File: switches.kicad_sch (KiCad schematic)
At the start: 9 parts, among them J13 Switch Assembly

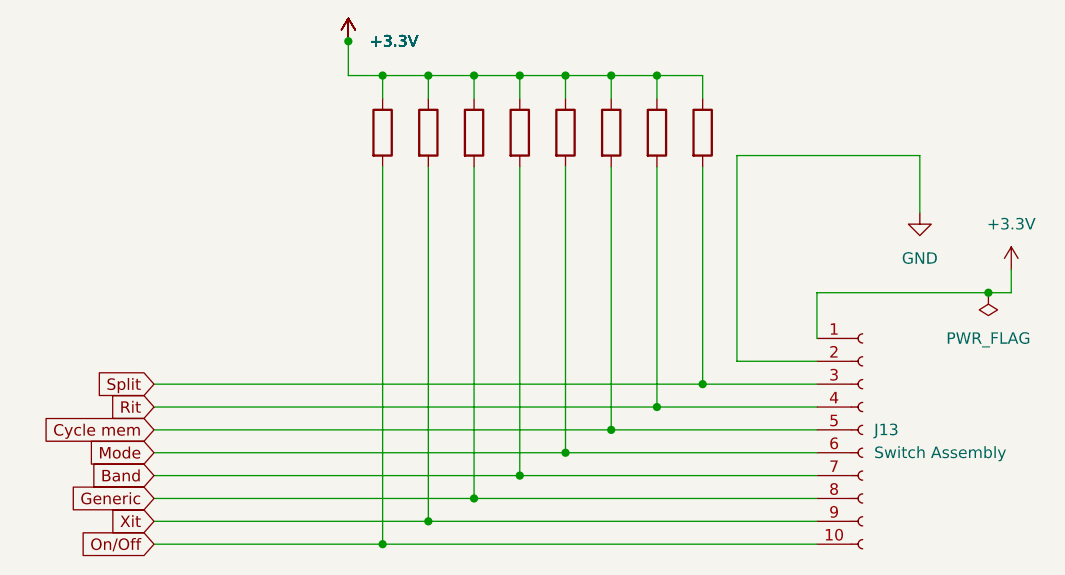
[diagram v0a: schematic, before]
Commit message: cont routing work
Changes:

* Added mounting holes
* Tried to trim down PCB size a litle more.
* Attempted to separate digital IO from analog.
* Added socket IC for RJ45 & 6P6C / RJ12 configurability.
* WIP: Add muxer for UART line switching.

Comment:

The muxer UART functionality isn't complete, the idea is to allow switching between using
the RJ45 RXD & TXD UART to the RJ12 / 6P6C UART lines.
Since the real rrc hardware supports this (depends on the radio configured) & maybe depending on socket strapping..
Need to add a jumper to enable switching between these, alternatively use a GPIO pin??
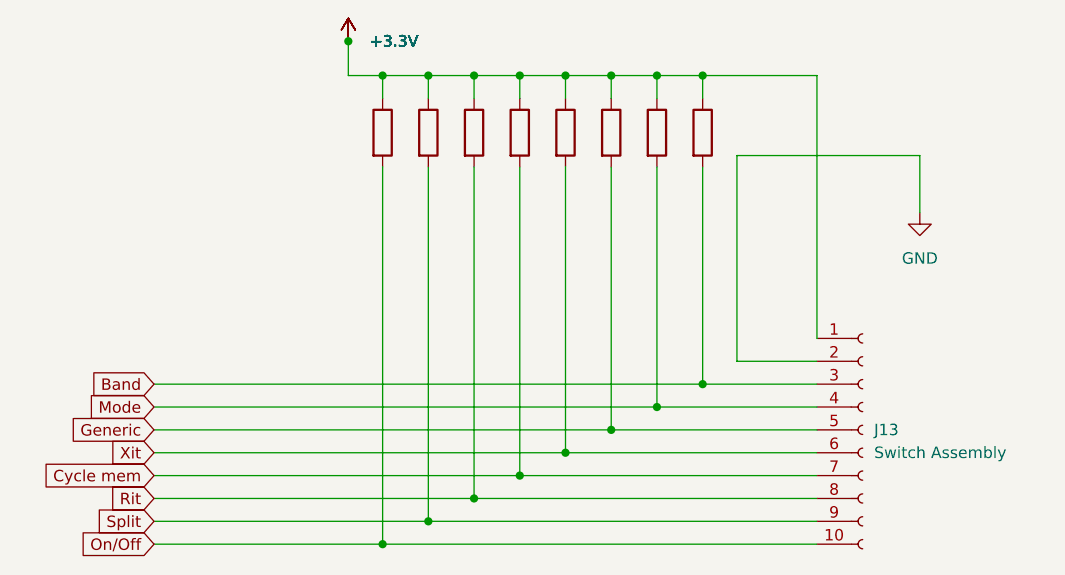
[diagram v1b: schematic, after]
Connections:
- net +3.3V is gone; now on net +3V3: J13.1 (Pin_1)
- net Band: now also J13.3 (Pin_3), R8.2; no longer J13.7 (Pin_7), R4.2
- net Cycle mem: now also J13.7 (Pin_7), R4.2; no longer J13.5 (Pin_5), R6.2
- net Generic: now also J13.5 (Pin_5), R6.2; no longer J13.8 (Pin_8), R3.2
- net Mode: now also J13.4 (Pin_4), R7.2; no longer J13.6 (Pin_6), R5.2
- net Rit: now also J13.8 (Pin_8), R3.2; no longer J13.4 (Pin_4), R7.2
- net Split: now also J13.9 (Pin_9), R2.2; no longer J13.3 (Pin_3), R8.2
- net Xit: now also J13.6 (Pin_6), R5.2; no longer J13.9 (Pin_9), R2.2
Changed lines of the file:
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@@
   (junction (at 144.78 55.88) (diameter 0) (color 0 0 0 0)
   )
+  (junction (at 154.94 55.88) (diameter 0) (color 0 0 0 0)
+  )
   (junction (at 124.46 105.41) (diameter 0) (color 0 0 0 0)
   )
@@
   (junction (at 154.94 90.17) (diameter 0) (color 0 0 0 0)
   )
-  (junction (at 186.69 80.01) (diameter 0) (color 0 0 0 0)
-  )
   (junction (at 139.7 97.79) (diameter 0) (color 0 0 0 0)
   )
@@
     (stroke (width 0) (type default))
   )
-  (wire (pts (xy 189.23 80.01) (xy 186.69 80.01))
-    (stroke (width 0) (type default))
-  )
   (wire (pts (xy 134.62 100.33) (xy 167.64 100.33))
     (stroke (width 0) (type default))
@@
     (stroke (width 0) (type default))
   )
-  (wire (pts (xy 189.23 77.47) (xy 189.23 80.01))
-    (stroke (width 0) (type default))
-  )
-  (wire (pts (xy 167.64 80.01) (xy 167.64 85.09))
-    (stroke (width 0) (type default))
-  )
   (wire (pts (xy 154.94 55.88) (xy 154.94 58.42))
     (stroke (width 0) (type default))
@@
     (stroke (width 0) (type default))
   )
+  (wire (pts (xy 167.64 85.09) (xy 167.64 55.88))
+    (stroke (width 0) (type default))
+  )
   (wire (pts (xy 119.38 107.95) (xy 167.64 107.95))
     (stroke (width 0) (type default))
@@
     (stroke (width 0) (type default))
   )
-  (wire (pts (xy 186.69 80.01) (xy 167.64 80.01))
-    (stroke (width 0) (type default))
-  )
   (wire (pts (xy 124.46 105.41) (xy 167.64 105.41))
     (stroke (width 0) (type default))
   )
+  (wire (pts (xy 167.64 55.88) (xy 154.94 55.88))
+    (stroke (width 0) (type default))
+  )
   (wire (pts (xy 129.54 66.04) (xy 129.54 102.87))
     (stroke (width 0) (type default))
@@
     (stroke (width 0) (type default))
   )
-  (global_label "Generic" (shape input) (at 93.98 102.87 180) (fields_autoplaced)
-    (effects (font (size 1.27 1.27)) (justify right))
-    (property "Intersheetrefs" "${INTERSHEET_REFS}" (at 83.919 102.87 0)
-      (effects (font (size 1.27 1.27)) (justify right) hide)
-    )
-  )
-  (global_label "Cycle mem" (shape input) (at 93.98 95.25 180) (fields_autoplaced)
-    (effects (font (size 1.27 1.27)) (justify right))
-    (property "Intersheetrefs" "${INTERSHEET_REFS}" (at 80.472 95.25 0)
-      (effects (font (size 1.27 1.27)) (justify right) hide)
-    )
-  )
-  (global_label "Mode" (shape input) (at 93.98 97.79 180) (fields_autoplaced)
-    (effects (font (size 1.27 1.27)) (justify right))
-    (property "Intersheetrefs" "${INTERSHEET_REFS}" (at 86.1568 97.79 0)
-      (effects (font (size 1.27 1.27)) (justify right) hide)
-    )
-  )
-  (global_label "Xit" (shape input) (at 93.98 105.41 180) (fields_autoplaced)
-    (effects (font (size 1.27 1.27)) (justify right))
-    (property "Intersheetrefs" "${INTERSHEET_REFS}" (at 88.4548 105.41 0)
-      (effects (font (size 1.27 1.27)) (justify right) hide)
-    )
-  )
-  (global_label "Band" (shape input) (at 93.98 100.33 180) (fields_autoplaced)
-    (effects (font (size 1.27 1.27)) (justify right))
-    (property "Intersheetrefs" "${INTERSHEET_REFS}" (at 86.2778 100.33 0)
+  (global_label "Mode" (shape input) (at 93.98 92.71 180) (fields_autoplaced)
+    (effects (font (size 1.27 1.27)) (justify right))
+    (property "Intersheetrefs" "${INTERSHEET_REFS}" (at 86.1568 92.71 0)
+      (effects (font (size 1.27 1.27)) (justify right) hide)
+    )
+  )
+  (global_label "Xit" (shape input) (at 93.98 97.79 180) (fields_autoplaced)
+    (effects (font (size 1.27 1.27)) (justify right))
+    (property "Intersheetrefs" "${INTERSHEET_REFS}" (at 88.4548 97.79 0)
+      (effects (font (size 1.27 1.27)) (justify right) hide)
+    )
+  )
+  (global_label "Band" (shape input) (at 93.98 90.17 180) (fields_autoplaced)
+    (effects (font (size 1.27 1.27)) (justify right))
+    (property "Intersheetrefs" "${INTERSHEET_REFS}" (at 86.2778 90.17 0)
+      (effects (font (size 1.27 1.27)) (justify right) hide)
+    )
+  )
+  (global_label "Split" (shape input) (at 93.98 105.41 180) (fields_autoplaced)
+    (effects (font (size 1.27 1.27)) (justify right))
+    (property "Intersheetrefs" "${INTERSHEET_REFS}" (at 86.6406 105.41 0)
       (effects (font (size 1.27 1.27)) (justify right) hide)
     )
@@
     )
   )
-  (global_label "Split" (shape input) (at 93.98 90.17 180) (fields_autoplaced)
-    (effects (font (size 1.27 1.27)) (justify right))
-    (property "Intersheetrefs" "${INTERSHEET_REFS}" (at 86.6406 90.17 0)
-      (effects (font (size 1.27 1.27)) (justify right) hide)
-    )
-  )
-  (global_label "Rit" (shape input) (at 93.98 92.71 180) (fields_autoplaced)
-    (effects (font (size 1.27 1.27)) (justify right))
-    (property "Intersheetrefs" "${INTERSHEET_REFS}" (at 88.3943 92.71 0)
+  (global_label "Cycle mem" (shape input) (at 93.98 100.33 180) (fields_autoplaced)
+    (effects (font (size 1.27 1.27)) (justify right))
+    (property "Intersheetrefs" "${INTERSHEET_REFS}" (at 80.472 100.33 0)
+      (effects (font (size 1.27 1.27)) (justify right) hide)
+    )
+  )
+  (global_label "Rit" (shape input) (at 93.98 102.87 180) (fields_autoplaced)
+    (effects (font (size 1.27 1.27)) (justify right))
+    (property "Intersheetrefs" "${INTERSHEET_REFS}" (at 88.3943 102.87 0)
+      (effects (font (size 1.27 1.27)) (justify right) hide)
+    )
+  )
+  (global_label "Generic" (shape input) (at 93.98 95.25 180) (fields_autoplaced)
+    (effects (font (size 1.27 1.27)) (justify right))
+    (property "Intersheetrefs" "${INTERSHEET_REFS}" (at 83.919 95.25 0)
       (effects (font (size 1.27 1.27)) (justify right) hide)
     )
@@
         )
         (path "/e63e39d7-6ac0-4ffd-8aa3-1841a4541b55/70162407-566b-4f7c-a9de-663cf6ba5a25"
-          (reference "#PWR015") (unit 1)
+          (reference "#PWR014") (unit 1)
         )
       )
@@
         )
         (path "/e63e39d7-6ac0-4ffd-8aa3-1841a4541b55/70162407-566b-4f7c-a9de-663cf6ba5a25"
-          (reference "#PWR016") (unit 1)
+          (reference "#PWR015") (unit 1)
         )
       )
@@
         )
         (path "/e63e39d7-6ac0-4ffd-8aa3-1841a4541b55/70162407-566b-4f7c-a9de-663cf6ba5a25"
-          (reference "#PWR017") (unit 1)
+          (reference "#PWR016") (unit 1)
         )
       )
@@
         )
         (path "/e63e39d7-6ac0-4ffd-8aa3-1841a4541b55/70162407-566b-4f7c-a9de-663cf6ba5a25"
-          (reference "#PWR018") (unit 1)
+          (reference "#PWR017") (unit 1)
         )
       )
@@
         )
         (path "/e63e39d7-6ac0-4ffd-8aa3-1841a4541b55/70162407-566b-4f7c-a9de-663cf6ba5a25"
-          (reference "#PWR019") (unit 1)
+          (reference "#PWR018") (unit 1)
         )
       )
@@
   (symbol (lib_name "GND_1") (lib_id "power:GND") (at 179.07 71.12 0) (unit 1)
     (in_bom yes) (on_board yes) (dnp no) (fields_autoplaced)
-    (property "Reference" "#PWR023" (at 179.07 77.47 0)
+    (property "Reference" "#PWR022" (at 179.07 77.47 0)
       (effects (font (size 1.27 1.27)) hide)
     )
@@
       (project "rrc-interface"
         (path "/e63e39d7-6ac0-4ffd-8aa3-1841a4541b55/70162407-566b-4f7c-a9de-663cf6ba5a25"
-          (reference "#PWR023") (unit 1)
+          (reference "#PWR022") (unit 1)
         )
       )
@@
         )
         (path "/e63e39d7-6ac0-4ffd-8aa3-1841a4541b55/70162407-566b-4f7c-a9de-663cf6ba5a25"
-          (reference "#PWR020") (unit 1)
-        )
-      )
-    )
-  )
-  (symbol (lib_id "power:PWR_FLAG") (at 186.69 80.01 180) (unit 1)
-    (in_bom yes) (on_board yes) (dnp no) (fields_autoplaced)
-    (property "Reference" "#FLG04" (at 186.69 81.915 0)
-      (effects (font (size 1.27 1.27)) hide)
-    )
-    (property "Value" "PWR_FLAG" (at 186.69 85.09 0)
-      (effects (font (size 1.27 1.27)))
-    )
-    (property "Footprint" "" (at 186.69 80.01 0)
-      (effects (font (size 1.27 1.27)) hide)
-    )
-    (property "Datasheet" "~" (at 186.69 80.01 0)
-      (effects (font (size 1.27 1.27)) hide)
-    )
-    (pin "1")
-    (instances
-      (project "rrc-interface"
-        (path "/e63e39d7-6ac0-4ffd-8aa3-1841a4541b55/70162407-566b-4f7c-a9de-663cf6ba5a25"
-          (reference "#FLG04") (unit 1)
+          (reference "#PWR019") (unit 1)
         )
       )
@@
         )
         (path "/e63e39d7-6ac0-4ffd-8aa3-1841a4541b55/70162407-566b-4f7c-a9de-663cf6ba5a25"
-          (reference "#PWR021") (unit 1)
+          (reference "#PWR020") (unit 1)
         )
       )
@@
         )
         (path "/e63e39d7-6ac0-4ffd-8aa3-1841a4541b55/70162407-566b-4f7c-a9de-663cf6ba5a25"
-          (reference "#PWR022") (unit 1)
+          (reference "#PWR021") (unit 1)
         )
       )
@@
         )
       )
-    )
-  )
-  (symbol (lib_name "+3.3V_1") (lib_id "power:+3.3V") (at 189.23 77.47 0) (unit 1)
-    (in_bom yes) (on_board yes) (dnp no)
-    (property "Reference" "#PWR024" (at 189.23 81.28 0)
-      (effects (font (size 1.27 1.27)) hide)
-    )
-    (property "Value" "+3.3V" (at 189.23 72.39 0)
-      (effects (font (size 1.27 1.27)))
-    )
-    (property "Footprint" "" (at 189.23 77.47 0)
-      (effects (font (size 1.27 1.27)) hide)
-    )
-    (property "Datasheet" "" (at 189.23 77.47 0)
-      (effects (font (size 1.27 1.27)) hide)
-    )
-    (pin "1")
-    (instances
-      (project "rrc-interface"
-        (path "/e63e39d7-6ac0-4ffd-8aa3-1841a4541b55/70162407-566b-4f7c-a9de-663cf6ba5a25"
-          (reference "#PWR024") (unit 1)
-        )
-      )

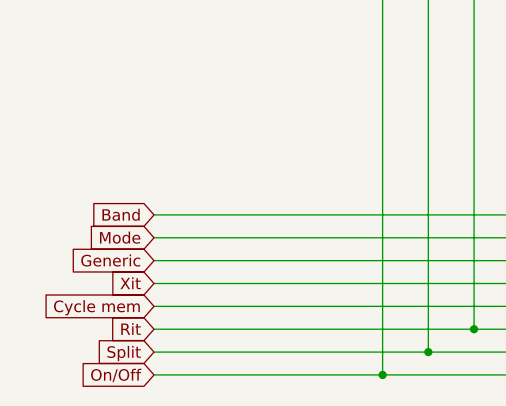
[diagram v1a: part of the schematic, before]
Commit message: add gnd pour to top layer, try to optimize routing
Changes:

* Opt to use normal via's instead of micro via's to reduce cost / production time.
* Add ground pour / plane to top layer.
* Reorganize component layout a bit to try to optimize paths.
* Change connector types to JST (will soon have a crimp kit for these connectors).
* Try to split the PCB into analog and digital sections.
* Add mounting holes.
* Increase track size for power traces.

TODO:

* Via stitching to make sure the resistance between planes is as low as possible?
* Configure board size.
* Finish variable resistor PCB's & add connectors to the PCB's for interconnect.
* Remove 3.5mm jacks from layout, need separate PCB's for these. Need to be able to mount the jack's on a panel, need flexibility.
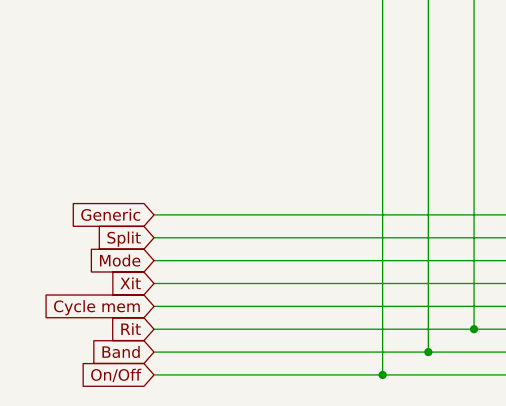
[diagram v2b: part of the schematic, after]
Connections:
- net Band: now also J13.9 (Pin_9), R2.2; no longer J13.3 (Pin_3), R8.2
- net Generic: now also J13.3 (Pin_3), R8.2; no longer J13.5 (Pin_5), R6.2
- net Mode: now also J13.5 (Pin_5), R6.2; no longer J13.4 (Pin_4), R7.2
- net Split: now also J13.4 (Pin_4), R7.2; no longer J13.9 (Pin_9), R2.2
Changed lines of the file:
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@@
     (stroke (width 0) (type default))
   )
-  (global_label "Mode" (shape input) (at 93.98 92.71 180) (fields_autoplaced)
+  (global_label "Generic" (shape input) (at 93.98 90.17 180) (fields_autoplaced)
     (effects (font (size 1.27 1.27)) (justify right))
-    (property "Intersheetrefs" "${INTERSHEET_REFS}" (at 86.1568 92.71 0)
+    (property "Intersheetrefs" "${INTERSHEET_REFS}" (at 83.919 90.17 0)
       (effects (font (size 1.27 1.27)) (justify right) hide)
     )
@@
     )
   )
-  (global_label "Band" (shape input) (at 93.98 90.17 180) (fields_autoplaced)
+  (global_label "Split" (shape input) (at 93.98 92.71 180) (fields_autoplaced)
     (effects (font (size 1.27 1.27)) (justify right))
-    (property "Intersheetrefs" "${INTERSHEET_REFS}" (at 86.2778 90.17 0)
-      (effects (font (size 1.27 1.27)) (justify right) hide)
-    )
-  )
-  (global_label "Split" (shape input) (at 93.98 105.41 180) (fields_autoplaced)
-    (effects (font (size 1.27 1.27)) (justify right))
-    (property "Intersheetrefs" "${INTERSHEET_REFS}" (at 86.6406 105.41 0)
+    (property "Intersheetrefs" "${INTERSHEET_REFS}" (at 86.6406 92.71 0)
       (effects (font (size 1.27 1.27)) (justify right) hide)
     )
@@
     )
   )
-  (global_label "Generic" (shape input) (at 93.98 95.25 180) (fields_autoplaced)
+  (global_label "Mode" (shape input) (at 93.98 95.25 180) (fields_autoplaced)
     (effects (font (size 1.27 1.27)) (justify right))
-    (property "Intersheetrefs" "${INTERSHEET_REFS}" (at 83.919 95.25 0)
+    (property "Intersheetrefs" "${INTERSHEET_REFS}" (at 86.1568 95.25 0)
       (effects (font (size 1.27 1.27)) (justify right) hide)
     )
+  )
+  (global_label "Band" (shape input) (at 93.98 105.41 180) (fields_autoplaced)
+    (effects (font (size 1.27 1.27)) (justify right))
+    (property "Intersheetrefs" "${INTERSHEET_REFS}" (at 86.2778 105.41 0)
+      (effects (font (size 1.27 1.27)) (justify right) hide)
+    )

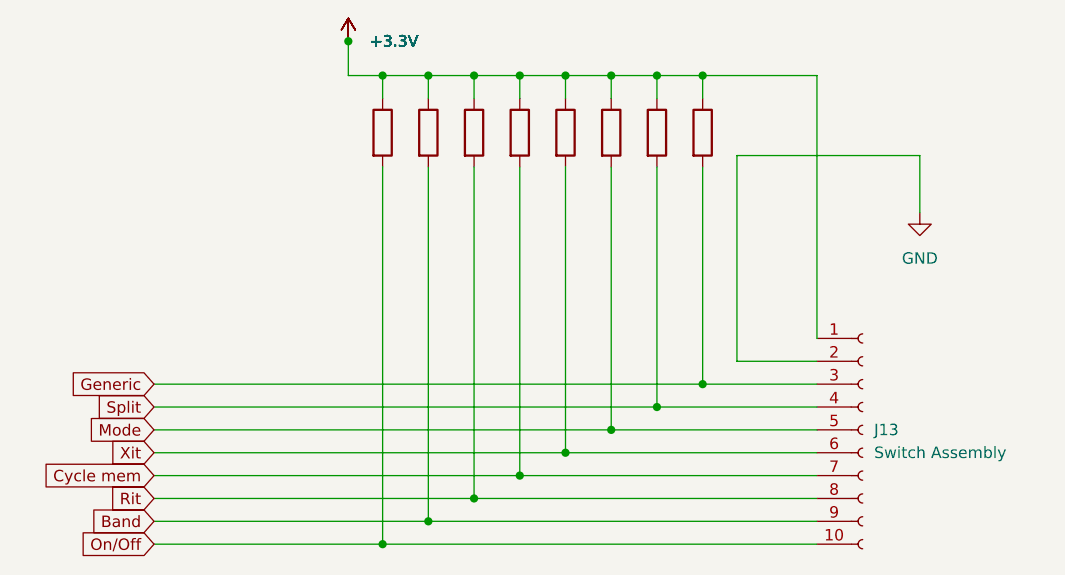
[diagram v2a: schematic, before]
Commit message: update main board routing, add 3d models and improve layout
Changes:

* update main board layout a bit
* try to improve routing
* add 3d model for 6p6c
* add decoupling caps to ptt line
* almost finish pot board
* switch board almost finished

Details:
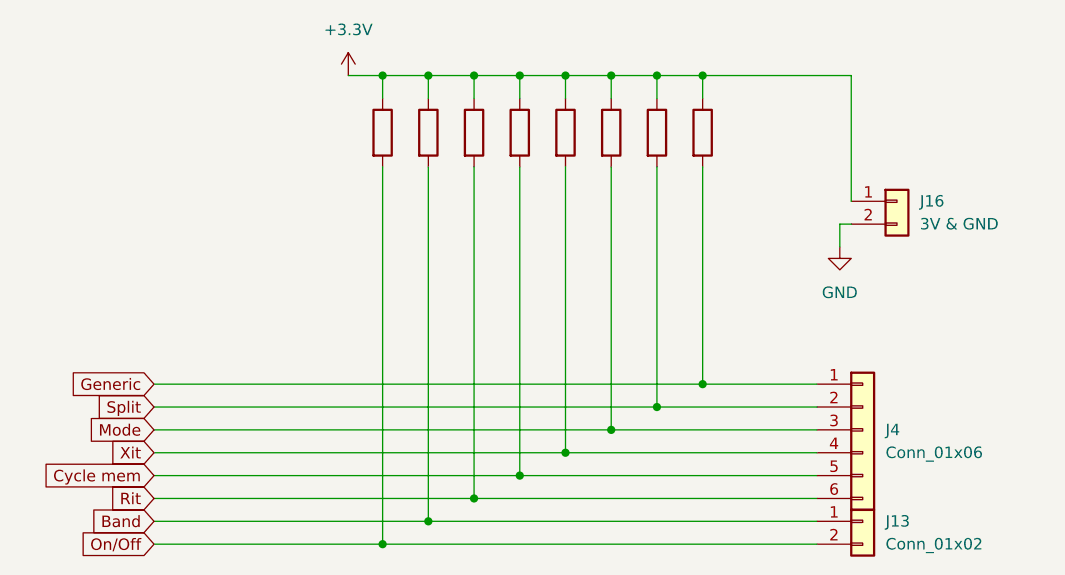
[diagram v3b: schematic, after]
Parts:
- removed J13: Switch Assembly, Connector_Molex:Molex_KK-254_AE-6410-10A_1x10_P2.54mm_Vertical, symbol Connector:Conn_01x10_Socket
- added J13: Conn_01x02, Connector_JST:JST_PH_B2B-PH-K_1x02_P2.00mm_Vertical, symbol Connector_Generic:Conn_01x02
- added J16: 3V & GND, Connector_JST:JST_PH_B2B-PH-K_1x02_P2.00mm_Vertical, symbol Connector_Generic:Conn_01x02
- added J4: Conn_01x06, Connector_JST:JST_PH_B6B-PH-K_1x06_P2.00mm_Vertical, symbol Connector_Generic:Conn_01x06
- renumbered R5 to R?, R2 to R?, R8 to R?, R3 to R?, R6 to R?, R1 to R?, R7 to R?, R4 to R?
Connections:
- net Band: now also J13.1 (Pin_1)
- net Cycle mem: now also J4.5 (Pin_5)
- net GND: now also J16.2 (Pin_2)
- net Generic: now also J4.1 (Pin_1)
- net Mode: now also J4.3 (Pin_3)
- net On/Off: now also J13.2 (Pin_2)
- net Rit: now also J4.6 (Pin_6)
- net Split: now also J4.2 (Pin_2)
- net Xit: now also J4.4 (Pin_4)
- net +3V3 renamed +3.3V
- net +3.3V: now also J16.1 (Pin_1)
